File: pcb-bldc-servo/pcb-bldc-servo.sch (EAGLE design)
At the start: 53 parts, among them J1 03-JST-B3B-XH-A, J2 03-JST-B3B-XH-A, J9 03-JST-B3B-XH-A, T1 MMBT2222, U1 AS5600, U2 STM32F030CCT6, X1 04-JST-B4B-XH-A, X2 PIN_6X1, X5 PIN_5X1HD

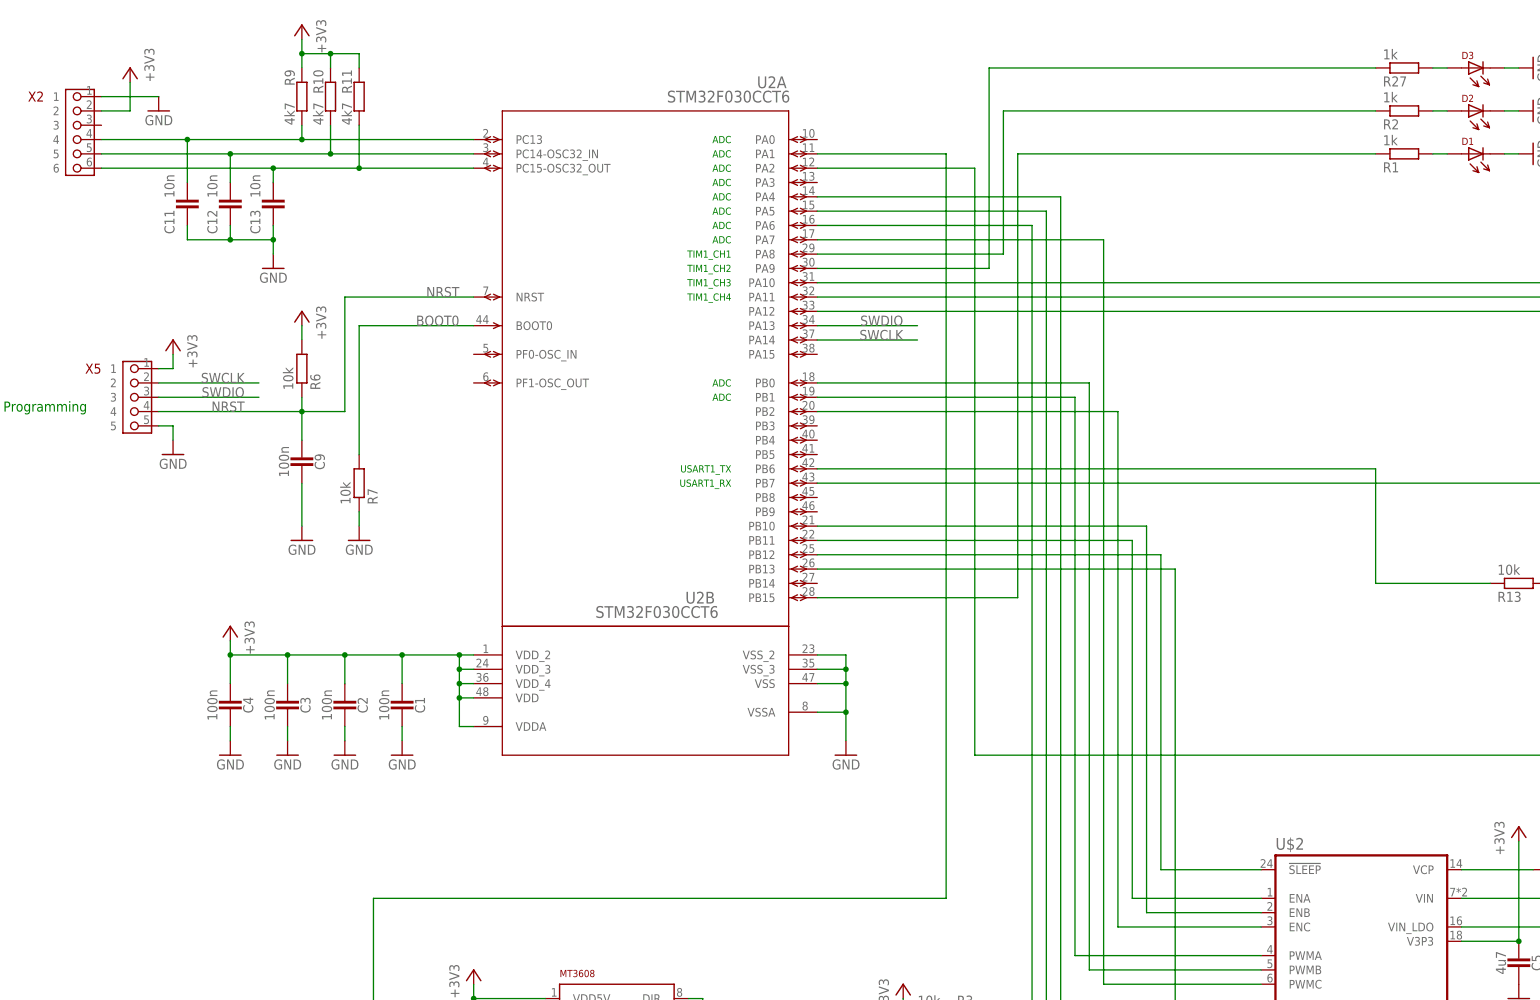
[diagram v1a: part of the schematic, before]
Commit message: updated schematic for correct sensor cable
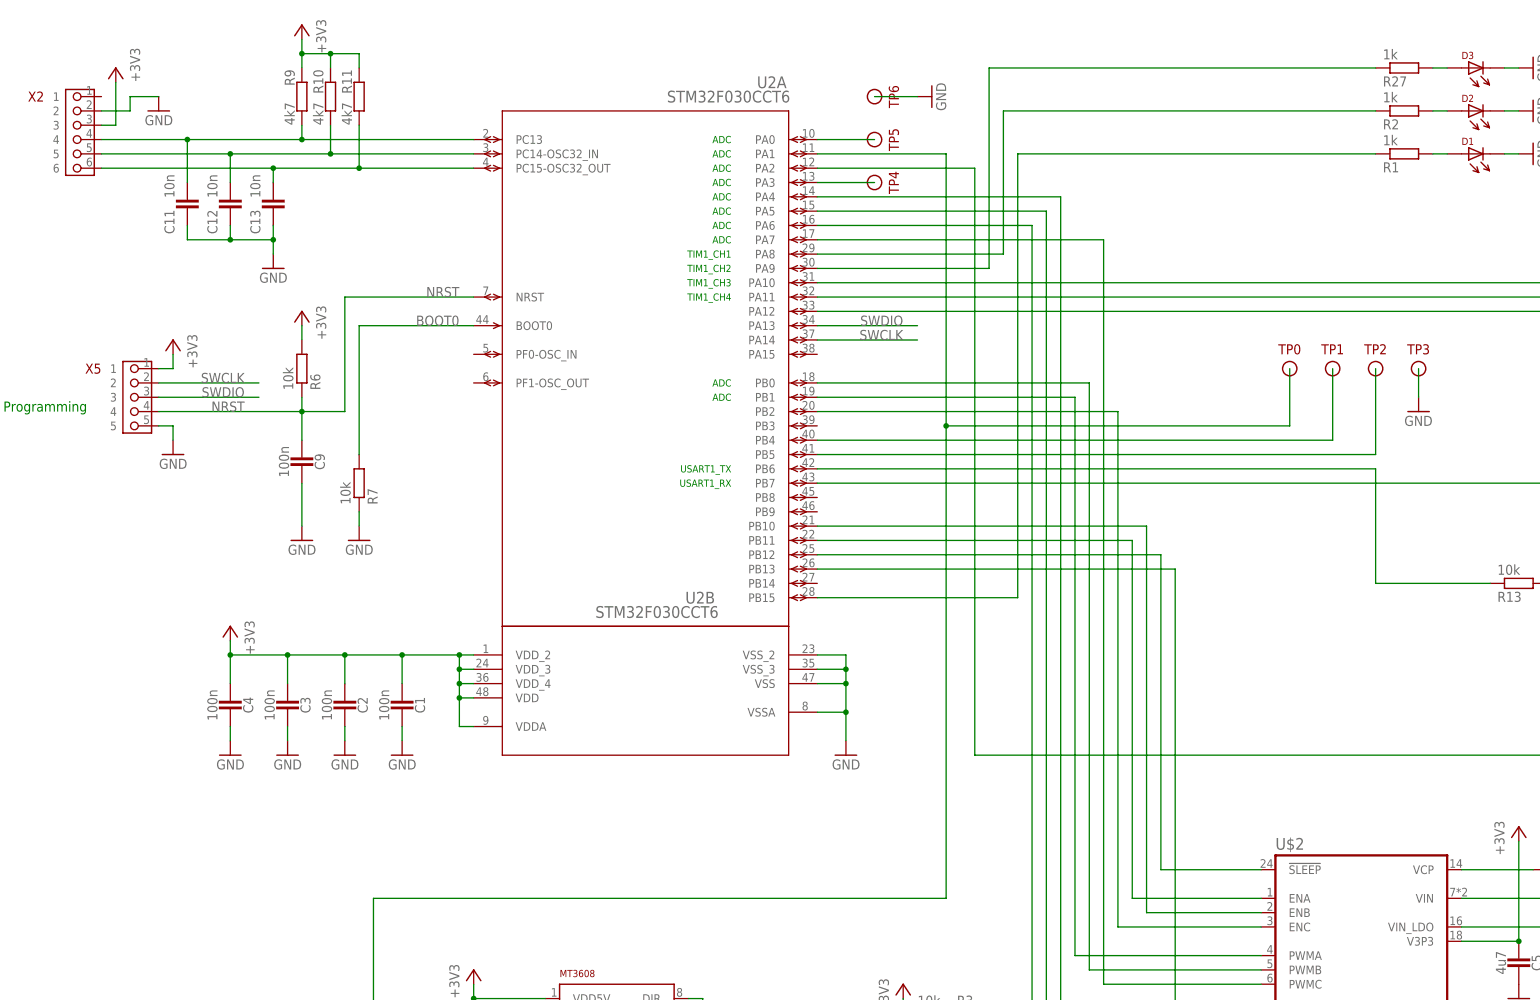
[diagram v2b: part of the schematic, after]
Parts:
- added TP0, TP1, TP2, TP3, TP4, TP5, TP6: TESTPIN, ftobler:TESTPIN
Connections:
- new net N$31: TP1.1, U2A.PB4
- new net N$33: TP2.1, U2A.PB5
- new net N$34: TP4.1, U2A.PA3
- new net N$35: TP5.1, U2A.PA0
- net +3V3: now also X2.3; no longer X2.2
- net GND: now also TP3.1, TP6.1, X2.2; no longer X2.1
- net N$32: now also TP0.1
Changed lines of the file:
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@@
 <part name="V3" library="ftobler" deviceset="FIDUCIAL" device="2MM"/>
 <part name="V4" library="ftobler" deviceset="FIDUCIAL" device="2MM"/>
+<part name="TP1" library="ftobler" deviceset="TESTPIN" device="" package3d_urn="urn:adsk.eagle:package:36843744/2"/>
+<part name="TP2" library="ftobler" deviceset="TESTPIN" device="" package3d_urn="urn:adsk.eagle:package:36843744/2"/>
+<part name="TP3" library="ftobler" deviceset="TESTPIN" device="" package3d_urn="urn:adsk.eagle:package:36843744/2"/>
+<part name="GND21" library="supply1" library_urn="urn:adsk.eagle:library:371" deviceset="GND" device=""/>
+<part name="TP0" library="ftobler" deviceset="TESTPIN" device="" package3d_urn="urn:adsk.eagle:package:36843744/2"/>
+<part name="TP4" library="ftobler" deviceset="TESTPIN" device="" package3d_urn="urn:adsk.eagle:package:36843744/2"/>
+<part name="TP5" library="ftobler" deviceset="TESTPIN" device="" package3d_urn="urn:adsk.eagle:package:36843744/2"/>
+<part name="TP6" library="ftobler" deviceset="TESTPIN" device="" package3d_urn="urn:adsk.eagle:package:36843744/2"/>
+<part name="GND22" library="supply1" library_urn="urn:adsk.eagle:library:371" deviceset="GND" device=""/>
 </parts>
 <sheets>
@@
 <attribute name="NAME" x="12.7" y="243.84" size="1.778" layer="94" rot="MR0" align="center-left"/>
 </instance>
-<instance part="+3V5" gate="G$1" x="27.94" y="248.92" smashed="yes" rot="MR0">
-<attribute name="VALUE" x="30.48" y="246.38" size="1.778" layer="96" rot="MR90"/>
+<instance part="+3V5" gate="G$1" x="25.4" y="248.92" smashed="yes" rot="MR0">
+<attribute name="VALUE" x="27.94" y="246.38" size="1.778" layer="96" rot="MR90"/>
 </instance>
 <instance part="GND15" gate="1" x="33.02" y="241.3" smashed="yes" rot="MR0">
@@
 <instance part="V4" gate="G$1" x="205.74" y="12.7" smashed="yes">
 <attribute name="NAME" x="205.74" y="15.748" size="1.27" layer="94" align="bottom-center"/>
+</instance>
+<instance part="TP1" gate="G$1" x="241.3" y="195.58" smashed="yes">
+<attribute name="NAME" x="241.3" y="198.12" size="1.778" layer="94" align="bottom-center"/>
+</instance>
+<instance part="TP2" gate="G$1" x="248.92" y="195.58" smashed="yes">
+<attribute name="NAME" x="248.92" y="198.12" size="1.778" layer="94" align="bottom-center"/>
+</instance>
+<instance part="TP3" gate="G$1" x="256.54" y="195.58" smashed="yes">
+<attribute name="NAME" x="256.54" y="198.12" size="1.778" layer="94" align="bottom-center"/>
+</instance>
+<instance part="GND21" gate="1" x="256.54" y="187.96" smashed="yes">
+<attribute name="VALUE" x="254" y="185.42" size="1.778" layer="96"/>
+</instance>
+<instance part="TP0" gate="G$1" x="233.68" y="195.58" smashed="yes">
+<attribute name="NAME" x="233.68" y="198.12" size="1.778" layer="94" align="bottom-center"/>
+</instance>
+<instance part="TP4" gate="G$1" x="160.02" y="228.6" smashed="yes" rot="R270">
+<attribute name="NAME" x="162.56" y="228.6" size="1.778" layer="94" rot="R270" align="bottom-center"/>
+</instance>
+<instance part="TP5" gate="G$1" x="160.02" y="236.22" smashed="yes" rot="R270">
+<attribute name="NAME" x="162.56" y="236.22" size="1.778" layer="94" rot="R270" align="bottom-center"/>
+</instance>
+<instance part="TP6" gate="G$1" x="160.02" y="243.84" smashed="yes" rot="R270">
+<attribute name="NAME" x="162.56" y="243.84" size="1.778" layer="94" rot="R270" align="bottom-center"/>
+</instance>
+<instance part="GND22" gate="1" x="170.18" y="243.84" smashed="yes" rot="R90">
+<attribute name="VALUE" x="172.72" y="241.3" size="1.778" layer="96" rot="R90"/>
 </instance>
 </instances>
@@
 </segment>
 <segment>
-<pinref part="X2" gate="G$1" pin="2"/>
-<wire x1="22.86" y1="241.3" x2="27.94" y2="241.3" width="0.1524" layer="91"/>
-<pinref part="+3V5" gate="G$1" pin="+3V3"/>
-<wire x1="27.94" y1="241.3" x2="27.94" y2="246.38" width="0.1524" layer="91"/>
-</segment>
-<segment>
 <pinref part="R9" gate="G$1" pin="1"/>
 <pinref part="+3V6" gate="G$1" pin="+3V3"/>
@@
 <wire x1="88.9" y1="86.36" x2="88.9" y2="83.82" width="0.1524" layer="91"/>
 <junction x="88.9" y="83.82"/>
+</segment>
+<segment>
+<pinref part="X2" gate="G$1" pin="3"/>
+<wire x1="22.86" y1="238.76" x2="25.4" y2="238.76" width="0.1524" layer="91"/>
+<pinref part="+3V5" gate="G$1" pin="+3V3"/>
+<wire x1="25.4" y1="238.76" x2="25.4" y2="246.38" width="0.1524" layer="91"/>
 </segment>
 </net>
@@
 </segment>
 <segment>
-<pinref part="X2" gate="G$1" pin="1"/>
-<wire x1="22.86" y1="243.84" x2="33.02" y2="243.84" width="0.1524" layer="91"/>
-<pinref part="GND15" gate="1" pin="GND"/>
-</segment>
-<segment>
 <pinref part="D2" gate="G$1" pin="2"/>
 <pinref part="GND28" gate="1" pin="GND"/>
@@
 <pinref part="C15" gate="G$1" pin="2"/>
 <pinref part="GND20" gate="1" pin="GND"/>
+</segment>
+<segment>
+<pinref part="TP3" gate="G$1" pin="1"/>
+<pinref part="GND21" gate="1" pin="GND"/>
+<wire x1="256.54" y1="195.58" x2="256.54" y2="190.5" width="0.1524" layer="91"/>
+</segment>
+<segment>
+<pinref part="TP6" gate="G$1" pin="1"/>
+<pinref part="GND22" gate="1" pin="GND"/>
+<wire x1="160.02" y1="243.84" x2="167.64" y2="243.84" width="0.1524" layer="91"/>
+</segment>
+<segment>
+<pinref part="X2" gate="G$1" pin="2"/>
+<wire x1="22.86" y1="241.3" x2="27.94" y2="241.3" width="0.1524" layer="91"/>
+<wire x1="27.94" y1="241.3" x2="27.94" y2="243.84" width="0.1524" layer="91"/>
+<pinref part="GND15" gate="1" pin="GND"/>
+<wire x1="27.94" y1="243.84" x2="33.02" y2="243.84" width="0.1524" layer="91"/>
 </segment>
 </net>
@@
 <wire x1="71.12" y1="78.74" x2="71.12" y2="101.6" width="0.1524" layer="91"/>
 <wire x1="71.12" y1="101.6" x2="172.72" y2="101.6" width="0.1524" layer="91"/>
-<wire x1="172.72" y1="101.6" x2="172.72" y2="233.68" width="0.1524" layer="91"/>
+<wire x1="172.72" y1="101.6" x2="172.72" y2="185.42" width="0.1524" layer="91"/>
 <pinref part="U2" gate="A" pin="PA1"/>
+<wire x1="172.72" y1="185.42" x2="172.72" y2="233.68" width="0.1524" layer="91"/>
 <wire x1="172.72" y1="233.68" x2="149.86" y2="233.68" width="0.1524" layer="91"/>
 <pinref part="C15" gate="G$1" pin="1"/>
 <wire x1="78.74" y1="76.2" x2="78.74" y2="78.74" width="0.1524" layer="91"/>
 <junction x="78.74" y="78.74"/>
-</segment>
-</net>
+<pinref part="TP0" gate="G$1" pin="1"/>
+<wire x1="233.68" y1="195.58" x2="233.68" y2="185.42" width="0.1524" layer="91"/>
+<wire x1="233.68" y1="185.42" x2="172.72" y2="185.42" width="0.1524" layer="91"/>
+<junction x="172.72" y="185.42"/>
+</segment>
+</net>
+<net name="N$31" class="0">
+<segment>
+<pinref part="TP1" gate="G$1" pin="1"/>
+<pinref part="U2" gate="A" pin="PB4"/>
+<wire x1="241.3" y1="195.58" x2="241.3" y2="182.88" width="0.1524" layer="91"/>
+<wire x1="241.3" y1="182.88" x2="149.86" y2="182.88" width="0.1524" layer="91"/>
+</segment>
+</net>
+<net name="N$33" class="0">
+<segment>
+<pinref part="U2" gate="A" pin="PB5"/>
+<pinref part="TP2" gate="G$1" pin="1"/>
+<wire x1="149.86" y1="180.34" x2="248.92" y2="180.34" width="0.1524" layer="91"/>
+<wire x1="248.92" y1="180.34" x2="248.92" y2="195.58" width="0.1524" layer="91"/>
+</segment>
+</net>
+<net name="N$34" class="0">
+<segment>
+<pinref part="TP4" gate="G$1" pin="1"/>
+<pinref part="U2" gate="A" pin="PA3"/>
+<wire x1="160.02" y1="228.6" x2="149.86" y2="228.6" width="0.1524" layer="91"/>
+</segment>
+</net>
+<net name="N$35" class="0">
+<segment>
+<pinref part="U2" gate="A" pin="PA0"/>
+<pinref part="TP5" gate="G$1" pin="1"/>
+<wire x1="149.86" y1="236.22" x2="160.02" y2="236.22" width="0.1524" layer="91"/>
+</segment>
+</net>
